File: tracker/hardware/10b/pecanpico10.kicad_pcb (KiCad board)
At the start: 2 copper layers, 23 x 50 mm, 121 parts, among them IC1 SPV1040T, IC10 AS213-92LF, IC2 TPS62260DRVR, IC3 ADP322ACPZ-115-R7, IC4 Si4464-B1B-FM, IC5 STM32F413RHT6, IC6 EVA-7M or EVA-M8, IC7 PAC1720-1-AIA-TR, IC8 TPS62260DRVR, IC9 BME280, J1 DM3AT-SF-PEJM5, J2 CONN_01X15, P1 CONN_01X25, P3 ZX62-B-5PA(33), P4 SMA, Q1 FDN306P, X1 KT2016K26000BCW18ZAS

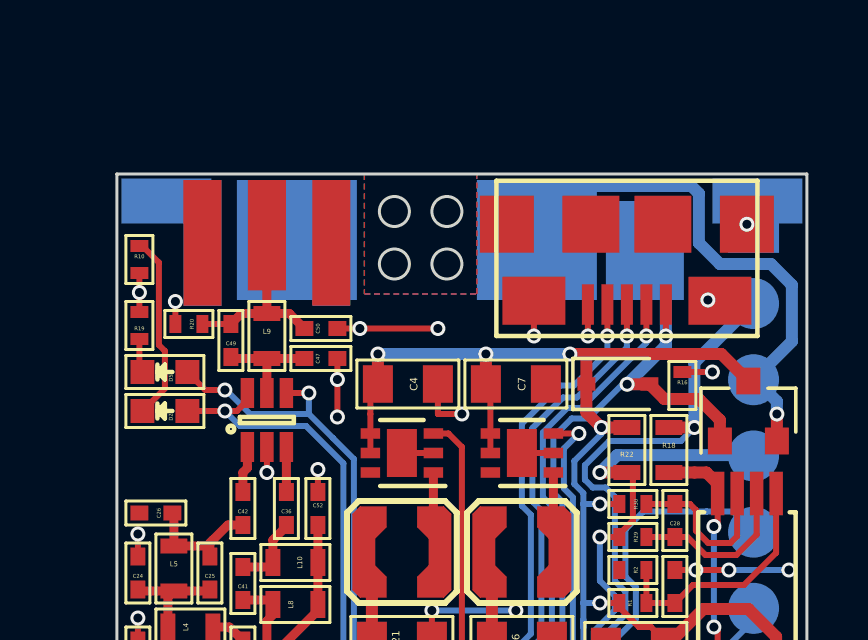
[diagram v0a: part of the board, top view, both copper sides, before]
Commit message: Fixed USB/battery isolation bug, increased schottky diode pad size
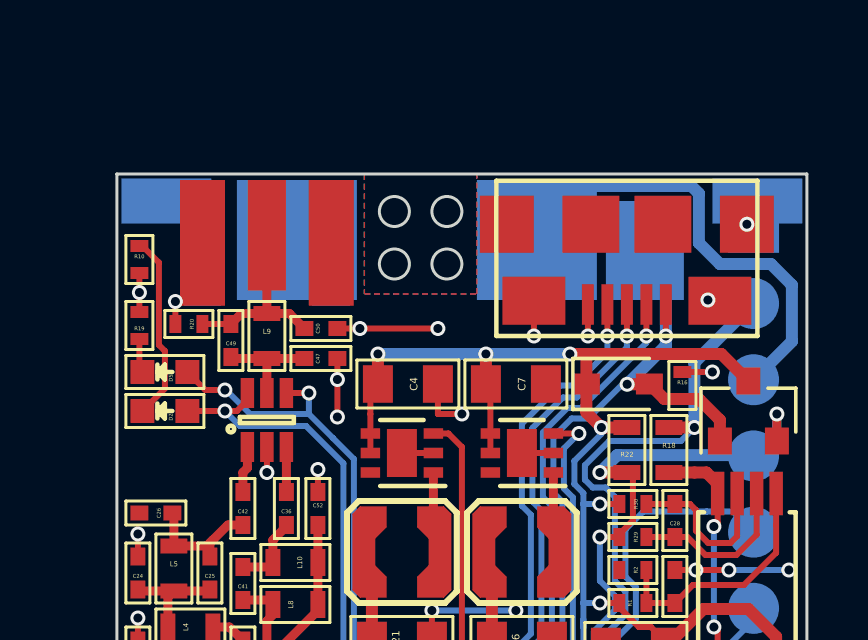
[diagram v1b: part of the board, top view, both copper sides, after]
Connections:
- net /IO_RXD renamed /IO_RXD_SDA
- net /IO_TXD renamed /IO_TXD_SCL
- J2 pad 3: /BATT_CONN -> Net-(J2-Pad3)
- Q1 pad 2: /BATT_CONN -> +BATT
- W11 pad 1: /BATT_CONN -> Net-(J2-Pad3)
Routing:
- net /BATT_CONN: track 17.6 -> 0.00 mm, vias 1 -> 0
- net Net-(J2-Pad3): track 0.00 -> 15.3 mm
- net +BATT: track 19.6 -> 22.2 mm, vias 3 -> 4

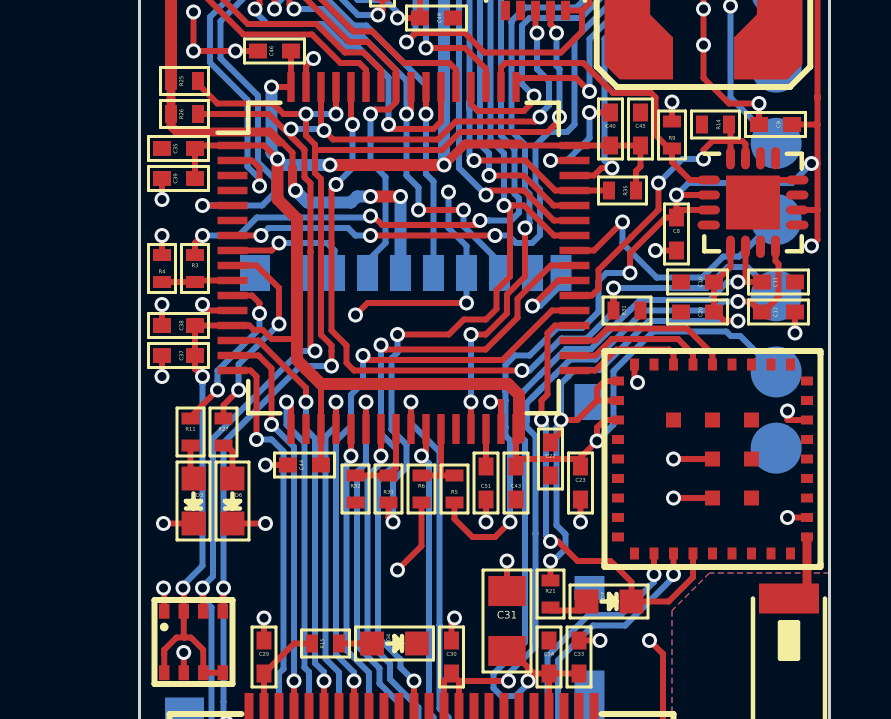
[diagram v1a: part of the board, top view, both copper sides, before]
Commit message: Added one more pin to pinheader
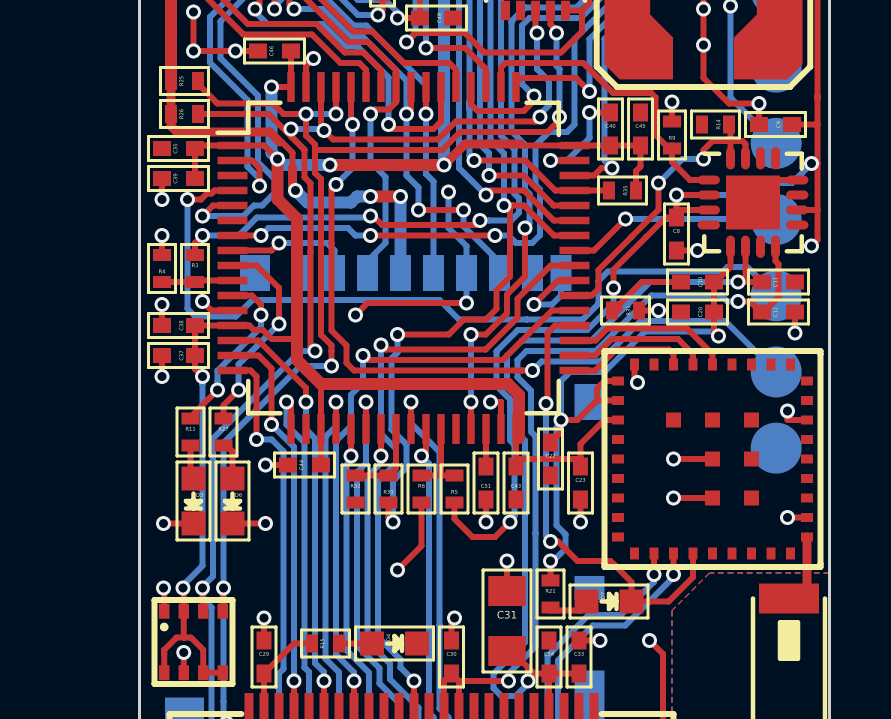
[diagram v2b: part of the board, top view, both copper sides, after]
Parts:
- moved R31 0.05 mm to (63.3, 107.3), turned to 180 degrees
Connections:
- IC5 pad 4: Net-(IC5-Pad4) -> /IO_PC15
- J2 pad 13: /BOOT0 -> /IO_PC15
- J2 pad 14: VCC -> /BOOT0
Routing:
- net /IO_PC15: track 0.00 -> 27.1 mm, vias 0 -> 1
- net VCC: track 90.9 -> 81.8 mm, vias 8 -> 7
- net GND: track 89.7 -> 92.6 mm
- net /IO_PA8: track 9.10 -> 7.16 mm
- net VDDA: track 43.1 -> 44.4 mm
- net /VCC_GPS: track 21.9 -> 21.1 mm
- net +1V8: track 26.6 -> 27.2 mm
- net /BOOT0: track 27.2 -> 26.5 mm
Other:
- net class Default: trace_width 0.3 -> 0.2
- board text added: "PA8/SCL"
- board text added: "PC15/ SDA"
- board text added: "Pecan Pico 10b"
- board text removed: "PA8"
- board text removed: "Pecan Pico 10a"
- board text removed: "VCORE"

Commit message: Relabeled pinheader
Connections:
- net /IO_RXD_SDA renamed /IO_RXD
- net /IO_TXD_SCL renamed /IO_TXD
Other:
- board text added: "+BATT"
- board text added: "+BATT-Pad"
- board text added: "+SOL"
- board text added: "Apr 2018"
- board text added: "I2C & GPIO"
- board text added: "SWD"
- board text added: "UART"
- board text removed: "Dec 2017"
- board text removed: "VBAT"
- board text removed: "VSOL"

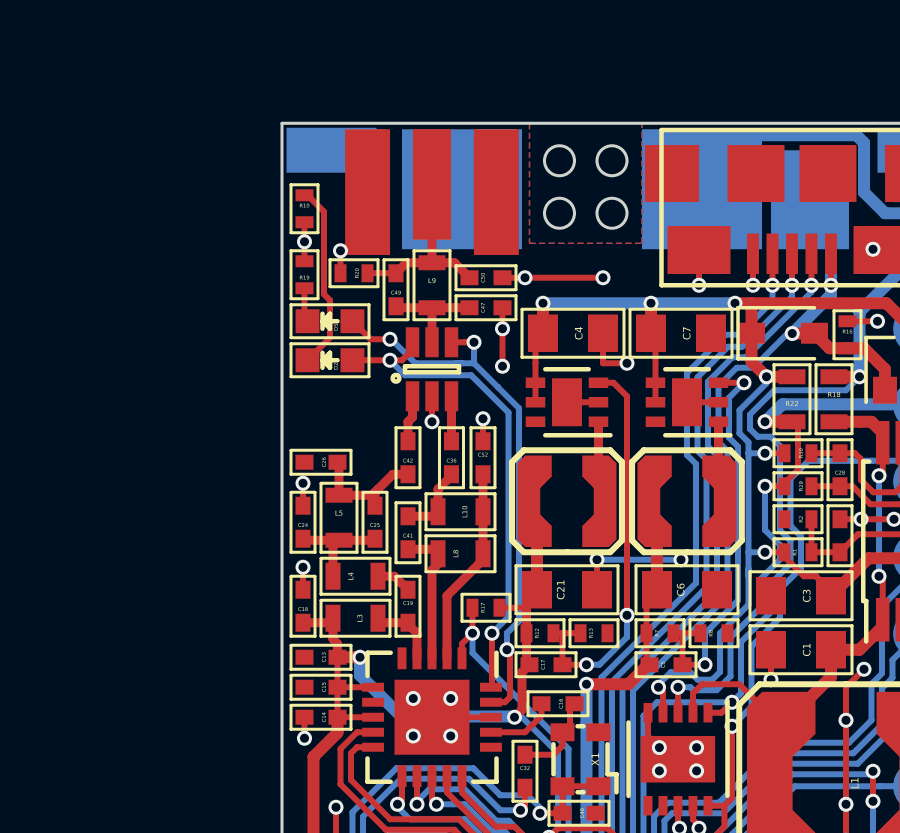
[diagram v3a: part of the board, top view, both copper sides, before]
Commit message: Moved LPF a bit backward
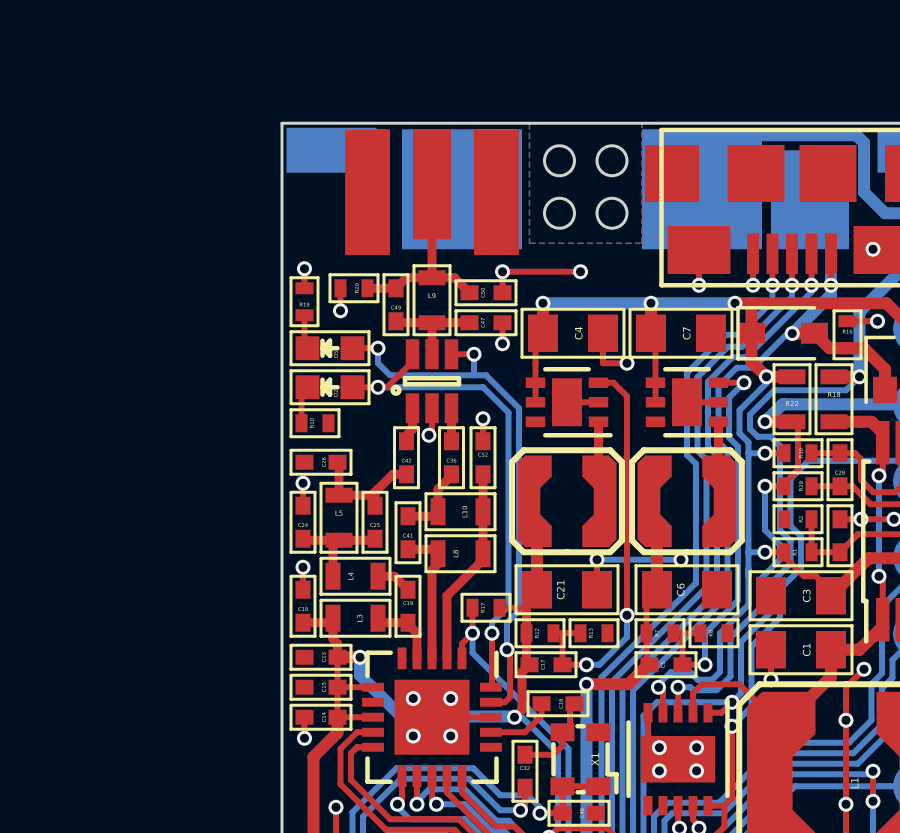
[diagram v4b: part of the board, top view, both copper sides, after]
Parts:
- moved R10 7.16 mm to (48.2, 84.6), turned to 0 degrees
- moved D2 0.90 mm to (48.7, 83.4)
- moved D5 0.90 mm to (48.7, 82.1)
- moved R19 0.90 mm to (47.9, 80.5)
- moved C47 0.50 mm to (53.9, 81.2)
- moved C49 0.50 mm to (50.9, 80.7)
- moved C50 0.50 mm to (53.9, 80.2)
- moved L9 0.50 mm to (52.1, 80.5)
- moved R20 0.50 mm to (49.5, 80.1)
- moved IC10 0.40 mm to (52.1, 83.2)
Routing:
- net Net-(D2-Pad1): track 6.22 -> 1.28 mm
- net GND: track 92.6 -> 90.7 mm, vias 73 -> 72
- net Net-(C49-Pad2): track 6.36 -> 6.86 mm
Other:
- net class Default: trace_width 0.2 -> 0.3

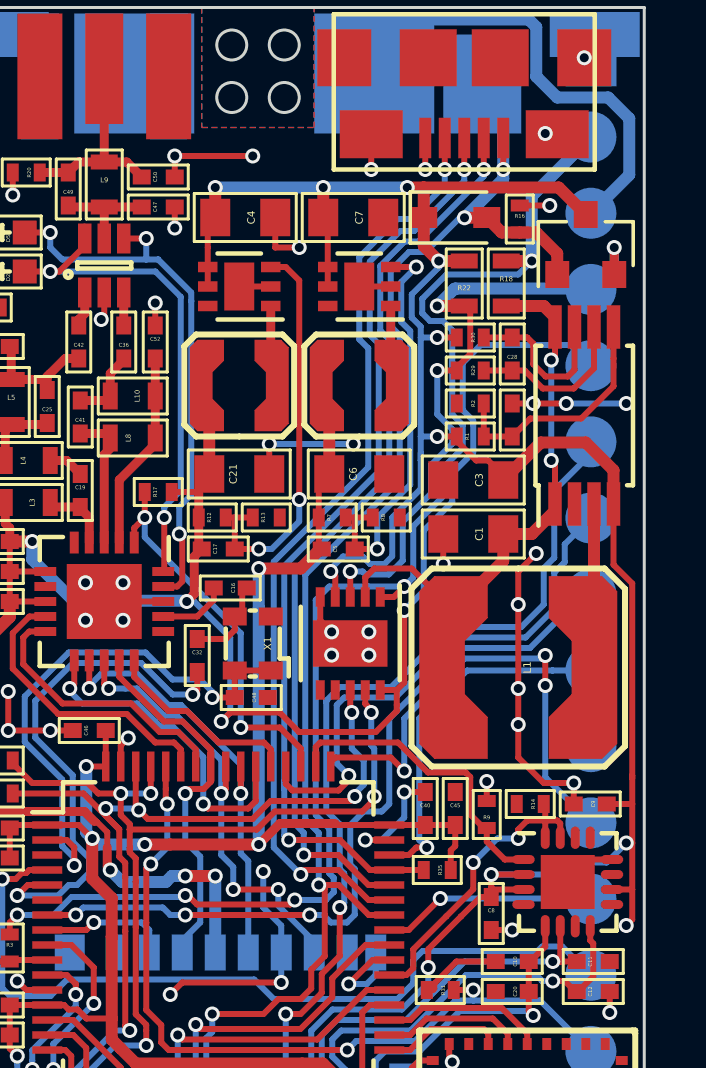
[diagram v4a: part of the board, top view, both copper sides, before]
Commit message: Fixed power measuring bug
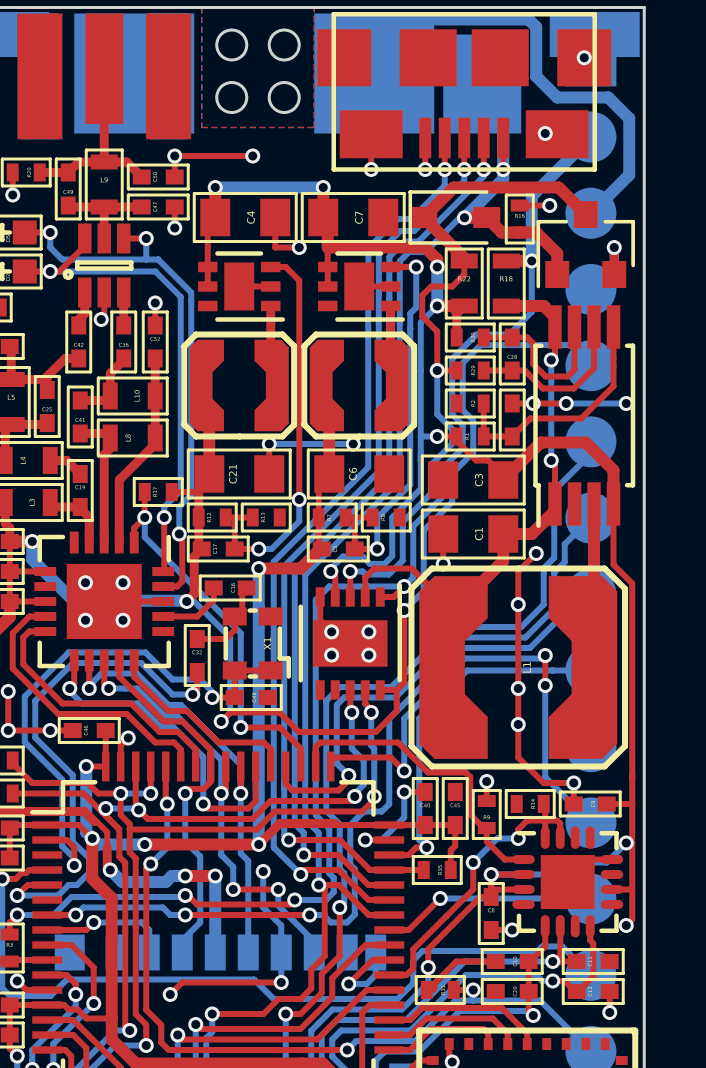
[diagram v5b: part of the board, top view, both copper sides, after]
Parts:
- turned R22 to 270 degrees
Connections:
- C3 pad 1: VDD -> /SENSE_BAT-
- C4 pad 2: VDD -> /SENSE_BAT-
- C7 pad 2: VDD -> /SENSE_BAT-
- C8 pad 1: VDD -> /SENSE_BAT-
- C9 pad 1: VDD -> /SENSE_BAT-
- IC1 pad 4: VDD -> /SENSE_BAT-
- IC2 pad 4: VDD -> /SENSE_BAT-
- IC2 pad 5: VDD -> /SENSE_BAT-
- IC3 pad 10: VDD -> /SENSE_BAT-
- IC3 pad 2: VDD -> /SENSE_BAT-
- IC3 pad 3: VDD -> /SENSE_BAT-
- IC7 pad 3: +BATT -> VDD
- IC7 pad 4: VDD -> /SENSE_BAT-
- IC8 pad 4: VDD -> /SENSE_BAT-
- IC8 pad 5: VDD -> /SENSE_BAT-
- R1 pad 1: VDD -> /SENSE_BAT-
- R22 pad 1: +BATT -> VDD
- R22 pad 2: VDD -> /SENSE_BAT-
- R29 pad 2: +BATT -> VDD
- R30 pad 2: VDD -> /SENSE_BAT-
- R5 pad 1: VDD -> /SENSE_BAT-
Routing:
- net /SENSE_BAT-: track 0.00 -> 81.2 mm, vias 0 -> 11
- net VDD: track 89.6 -> 24.0 mm, vias 12 -> 2
- net +BATT: track 22.2 -> 2.62 mm, vias 4 -> 1
- net +SOL: track 47.5 -> 45.3 mm
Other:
- net class Default: trace_width 0.3 -> 0.2

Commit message: Tidy up
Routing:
- net /SENSE_BAT-: track 81.2 -> 79.8 mm, vias 11 -> 10
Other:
- net class Default: trace_width 0.2 -> 0.4
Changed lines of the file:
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@@
     (thickness 1)
     (drawings 37)
-    (tracks 1646)
+    (tracks 1642)
     (zones 0)
     (modules 121)
@@
   )
   (setup
-    (last_trace_width 0.2)
+    (last_trace_width 0.4)
     (trace_clearance 0.149)
     (zone_clearance 0.15)
@@
   (net_class Default "This is the default net class."
     (clearance 0.149)
-    (trace_width 0.2)
+    (trace_width 0.4)
     (via_dia 0.5)
     (via_drill 0.3)
@@
   (segment (start 64.75 87.8) (end 64.75 88.9) (width 0.2) (layer F.Cu) (net 3))
   (segment (start 64.75 88.9) (end 65.7 88.9) (width 0.2) (layer F.Cu) (net 3))
+  (segment (start 60.3 94.25) (end 60.3 93.4) (width 0.2) (layer F.Cu) (net 4))
+  (segment (start 60.71501 93.4) (end 60.3 93.4) (width 0.2) (layer B.Cu) (net 4))
   (segment (start 63.2 86.7) (end 63.2 85.4) (width 0.2) (layer F.Cu) (net 4))
   (segment (start 63.2 85.4) (end 62.699999 84.899999) (width 0.2) (layer F.Cu) (net 4))
@@
   (segment (start 62.050011 93.034979) (end 61.584979 93.500011) (width 0.2) (layer B.Cu) (net 4))
   (segment (start 61.584979 93.500011) (end 60.815021 93.500011) (width 0.2) (layer B.Cu) (net 4))
-  (segment (start 60.71501 93.4) (end 60.3 93.4) (width 0.2) (layer B.Cu) (net 4))
-  (segment (start 60.3 93.4) (end 60.36501 93.4) (width 0.2) (layer B.Cu) (net 4))
   (via (at 60.3 93.4) (size 0.5) (drill 0.3) (layers F.Cu B.Cu) (net 4))
-  (segment (start 60.3 94.25) (end 60.3 93.45) (width 0.2) (layer F.Cu) (net 4))
-  (segment (start 60.3 93.45) (end 60.25 93.4) (width 0.2) (layer F.Cu) (net 4))
   (segment (start 63.2 86.7) (end 63.85 86.7) (width 0.2) (layer F.Cu) (net 4))
   (via (at 63.2 86.7) (size 0.5) (drill 0.3) (layers F.Cu B.Cu) (net 4))
@@
   (segment (start 49.150001 103.65) (end 48.7 103.65) (width 0.2) (layer F.Cu) (net 107))
   (via (at 48.7 103.65) (size 0.5) (drill 0.3) (layers F.Cu B.Cu) (net 107))
-  (segment (start 68.322 89.078) (end 68.322 89.478) (width 0.2) (layer B.Cu) (net 108))
-  (segment (start 67.1 92.940002) (end 66.74999 93.290012) (width 0.2) (layer B.Cu) (net 108))
-  (segment (start 68.322 89.478) (end 67.1 90.7) (width 0.2) (layer B.Cu) (net 108))
-  (segment (start 66.74999 94.500011) (end 66.000021 95.24998) (width 0.2) (layer B.Cu) (net 108))
-  (segment (start 67.1 90.7) (end 67.1 92.940002) (width 0.2) (layer B.Cu) (net 108))
-  (segment (start 66.74999 93.290012) (end 66.74999 94.500011) (width 0.2) (layer B.Cu) (net 108))
-  (segment (start 66.000021 95.24998) (end 63.665056 95.24998) (width 0.2) (layer B.Cu) (net 108))
-  (segment (start 63.665056 95.24998) (end 61.665047 97.249989) (width 0.2) (layer B.Cu) (net 108))
-  (segment (start 61.665047 97.249989) (end 59.955022 97.249989) (width 0.2) (layer B.Cu) (net 108))
-  (segment (start 59.955022 97.249989) (end 59.50005 97.704961) (width 0.2) (layer B.Cu) (net 108))
-  (segment (start 59.50005 97.704961) (end 59.50005 97.75) (width 0.2) (layer B.Cu) (net 108))
+  (segment (start 59.50005 97.75) (end 59.50005 97.704961) (width 0.2) (layer B.Cu) (net 108))
+  (segment (start 59.50005 97.704961) (end 59.955022 97.249989) (width 0.2) (layer B.Cu) (net 108))
+  (segment (start 59.955022 97.249989) (end 61.665047 97.249989) (width 0.2) (layer B.Cu) (net 108))
+  (segment (start 63.665056 95.24998) (end 66.000021 95.24998) (width 0.2) (layer B.Cu) (net 108))
+  (segment (start 61.665047 97.249989) (end 63.665056 95.24998) (width 0.2) (layer B.Cu) (net 108))
+  (segment (start 66.000021 95.24998) (end 66.74999 94.500011) (width 0.2) (layer B.Cu) (net 108))
+  (segment (start 68.322 89.116522) (end 68.322 89.078) (width 0.2) (layer B.Cu) (net 108))
+  (segment (start 66.74999 94.500011) (end 66.74999 93.290012) (width 0.2) (layer B.Cu) (net 108))
+  (segment (start 67.1 90.338522) (end 68.322 89.116522) (width 0.2) (layer B.Cu) (net 108))
+  (segment (start 66.74999 93.290012) (end 67.1 92.940002) (width 0.2) (layer B.Cu) (net 108))
+  (segment (start 67.1 92.940002) (end 67.1 90.338522) (width 0.2) (layer B.Cu) (net 108))
   (segment (start 58.15 108.15) (end 58.644988 108.15) (width 0.2) (layer F.Cu) (net 108))
   (segment (start 58.644988 108.15) (end 59.349989 107.444999) (width 0.2) (layer F.Cu) (net 108))
@@
   (segment (start 58.15 100.475002) (end 58.15 99.9) (width 0.2) (layer F.Cu) (net 109))
   (via (at 60.25 100.2) (size 0.5) (drill 0.3) (layers F.Cu B.Cu) (net 109))
+  (segment (start 69.7 102.45) (end 69.7 103.8) (width 0.2) (layer F.Cu) (net 110))
+  (segment (start 69.025 104) (end 69.5 104) (width 0.2) (layer F.Cu) (net 110))
+  (segment (start 69.7 103.8) (end 69.5 104) (width 0.2) (layer F.Cu) (net 110))
   (segment (start 59.55 82.6) (end 62.8 82.6) (width 0.4) (layer F.Cu) (net 110))
   (segment (start 62.8 82.6) (end 63.2 83) (width 0.4) (layer F.Cu) (net 110))
@@
   (segment (start 66.075 103.5) (end 65 103.5) (width 0.2) (layer F.Cu) (net 110))
   (segment (start 69.7 101.15) (end 69.7 102.45) (width 0.2) (layer F.Cu) (net 110))
-  (segment (start 69.7 102.45) (end 69.7 104) (width 0.2) (layer F.Cu) (net 110))
   (segment (start 69.5 102.45) (end 69.7 102.45) (width 0.2) (layer F.Cu) (net 110))
   (via (at 69.5 102.45) (size 0.5) (drill 0.3) (layers F.Cu B.Cu) (net 110))
-  (segment (start 69.7 104) (end 69.7 105) (width 0.2) (layer F.Cu) (net 110))
-  (segment (start 69.7 105) (end 69.5 105.2) (width 0.2) (layer F.Cu) (net 110))
   (via (at 65 103.5) (size 0.5) (drill 0.3) (layers F.Cu B.Cu) (net 110))
-  (segment (start 69.025 104) (end 69.7 104) (width 0.2) (layer F.Cu) (net 110))
-  (via (at 69.5 105.2) (size 0.5) (drill 0.3) (layers F.Cu B.Cu) (net 110))
   (segment (start 69.7 100.2) (end 69.7 93.8) (width 0.2) (layer F.Cu) (net 110))
   (segment (start 69.075 93.175) (end 69.7 93.8) (width 0.2) (layer F.Cu) (net 110))
